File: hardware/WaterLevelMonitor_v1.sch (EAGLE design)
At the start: 38 parts, among them J1 D24V5F5, J2 AVR_SPI_PRG_6PTH, J5 D24V5F5, J6 D24V5F5, J7 RJ45, Q1 NDP6020P, Q4 2N3904, U1 ATMEGA328P_PDIP

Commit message: Add files via upload
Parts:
- added D2: (no value), adafruit:DIODEDO-1N4148
- added J8: (no value), SparkFun-Connectors:M04PTH
- added J9: (no value), SparkFun-Connectors:M03PTH
- D1: value (none) -> 1N5819-B; device adafruit:DIODEDO-1N4148 -> diode:1N5819-B
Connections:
- removed net BATSW: R3.2
- new net N$12: J3.7, U1.PD4(XCK/T0)
- new net N$13: D2.C, J8.2
- new net N$15: D2.A, U1.PD0(RXD)
- new net N$16: J3.9, U1.PD3(INT1)
- new net N$17: J3.10, U1.PD2(INT0)
- new net N$18: J8.1, J9.2
- new net N$19: R3.2, U1.PC5(ADC5/SCL)
- new net N$7: J8.3, U1.PD1(TXD)
- net GND: now also J3.2, J8.4
- net N$4: now also J3.12
- net N$6: now also U1.PC0(ADC0)
- net VCC: now also J9.1
- net VCEL: now also J3.1
- net VSEN: now also J9.3
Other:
- note added: "Bat GND SPKR+ SPKR- Rst PS Key RI TX RX NS Vio"
- note added: "Hardware UART"
- note added: "V+ RXD TXD GND"
- moved on the sheet: C2, C3, C4, J3, R6

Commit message: Add files via upload
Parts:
- removed C3: 10uF, SparkFun-Capacitors:CAP_POLPTH1
- removed C5: 470uF, SparkFun-Capacitors:CAP_POLPTH4
- removed D11, D7, D8, D9: 6V Zener, SparkFun-DiscreteSemi:DIODE-ZENERPTH
- removed J11: (no value), SparkFun-Connectors:M02PTH
- removed LED1: (no value), adafruit:LED5MM
- removed R10: 330, resistor:R-US_0204/5
- removed R12: 46K, resistor:R-US_0204/5
- added C11, C12, C13: 330uF, SparkFun-Capacitors:CAP_POLPTH1
- added J16: (no value), SparkFun-Connectors:M08SILK_FEMALE_PTH
- added JP1: JUMPER-PAD-2-NOYES_SILK, SparkFun-Passives:JUMPER-PAD-2-NOYES_SILK
- C4: value 100uF -> 330uF
- D3: value 1N4001 -> (none); device SparkFun-DiscreteSemi:DIODEPTH -> adafruit:DIODEDO-1N4148
- J4: device SparkFun-Connectors:M01PTH -> SparkFun-Connectors:M05PTH
- J8: device SparkFun-Connectors:M04PTH -> SparkFun-Connectors:M05PTH
- J9: device SparkFun-Connectors:M03PTH -> SparkFun-Connectors:M05PTH
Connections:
- removed net N$12: J3.7, U1.PD4(XCK/T0)
- removed net N$13: D2.C, J8.2
- removed net N$17: J3.10, U1.PD2(INT0)
- removed net N$18: J8.1, J9.2
- removed net N$4 (its old number): C10.+, C6.2, C9.+, D1.C, J3.12, U1.AVCC, U1.VCC
- removed net N$7: J8.3, U1.PD1(TXD)
- removed net N$8: C5.+
- new net HWRXD: D2.C, J4.3
- new net HWTXD: J4.4, U1.PD1(TXD)
- new net MISO: J2.1, U1.PB4(MISO)
- new net MOSI: J2.4, U1.PB3(MOSI/OC2)
- new net N$20: D3.A, U1.PC2(ADC2)
- new net N$21: D3.C, J9.3
- new net N$22: J9.4, U1.PC3(ADC3)
- new net N$25: J8.3, U1.PC4(ADC4/SDA)
- new net N$26: J8.4, U1.PC5(ADC5/SCL)
- new net N$27: J16.1, J7.1
- new net N$28: J16.2, J7.2
- new net N$29: J16.3, J7.3
- new net N$30: J16.4, J7.4
- new net N$31: J16.5, J7.5
- new net N$32: J2.5, U1.PC6(/RESET)
- new net N$33: J16.6, J7.6
- new net N$34: J16.7, J7.7
- new net N$35: J16.8, J7.8
- new net SCK: J2.3, U1.PB5(SCK)
- new net SS: U1.PB2(SS/OC1B)
- new net VMCU: D1.A, J1.4
- net GND: now also C11.-, C12.-, C13.-, J2.6, J4.5, J8.5, J9.5; no longer C3.-, C5.-, D11.A, D7.A, D8.A, D9.A, J11.1, J8.4, LED1.C, R12.1
- net N$1: now also J3.7, U1.PD5(T1); no longer LED1.A, R10.2
- net N$19: now also U1.PC1(ADC1); no longer U1.PC5(ADC5/SCL)
- net N$5: now also J3.10, U1.PD4(XCK/T0); no longer R12.2
- net VBAT: now also JP1.1
- net VBATSW: now also C13.+, C4.+
- net VCC: now also C10.+, C6.2, C9.+, D1.C, J2.2, J3.12, J4.2, J8.2, J9.2, U1.AVCC, U1.VCC; no longer D1.A, J1.4, J9.1
- net VCEL: now also C11.+, C12.+, JP1.2
- net VSEN: now also J4.1, J8.1, J9.1; no longer J9.3
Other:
- note added: "Debug Console"
- note added: "HW UART"
- note added: "I2C"
- note added: "VSEN VCC RXD TXD GND"
- note added: "VSEN VCC SDA SCL GND"
- note removed: "1 GND 2 RESET 3 VCC (5V) 4 motion detector 5 photocell 6 on/off button 7 UART Rx 8 UART Tx"
- note removed: "Hardware UART"
- note removed: "LED Indicators"
- note removed: "V+ RXD TXD GND"
- moved on the sheet: C2, C4, D2, D6, J1, J2, J3, J5, J6, J7, Q1, Q4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

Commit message: Add files via upload
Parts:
- added J10, J11: (no value), SparkFun-Connectors:M01PTH_NO_SILK_YES_STOP
- added J12: (no value), SparkFun-Connectors:M031X03_NO_SILK
- added J13, J14, J15: (no value), SparkFun-Connectors:M02PTH
- added J17: (no value), SparkFun-Connectors:M04X2
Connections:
- removed net SS: U1.PB2(SS/OC1B)
- new net N$13: J10.1, J3.6
- new net N$37: J12.2, U1.PD7(AIN1)
- new net N$38: J12.3, U1.PB0(ICP)
- new net N$5: J11.1, U1.PD2(INT0)
- new net N$8: J12.1, U1.PD6(AIN0)
- new net SS1: J17.5, U1.PB2(SS/OC1B)
- new net SS2: J17.7, U1.PB1(OC1A)
- net GND: now also J13.2, J14.2, J15.2, J17.6
- net MISO: now also J17.1
- net MOSI: now also J17.4
- net SCK: now also J17.3
- net VCC: now also J14.1, J17.2
- net VMCU: now also J15.1
- net VSEN: now also J13.1, J17.8
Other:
- note added: "SPI"
- moved on the sheet: J3, J4, J8, J9

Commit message: Add files via upload
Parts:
- removed C12, C13: 330uF, SparkFun-Capacitors:CAP_POLPTH1
- removed Q4: 2N3904, SparkFun-DiscreteSemi:TRANSISTOR_NPNTO-92-AMMO
- removed R7: 10K, resistor:R-US_0204/5
- added C3: 0.1uF, SparkFun-Capacitors:CAPPTH
- added C5: 20pF, SparkFun-Capacitors:CAPPTH
- added J18: (no value), SparkFun-Connectors:M02PTH
- added J19: (no value), SparkFun-Connectors:M01PTH_NO_SILK_YES_STOP
- added J20, J22: (no value), SparkFun-Connectors:M021X02_NO_SILK
- added LED1: (no value), led:LED5MM
- added Q3: NDP6020P, transistor-power:PMOSFET_PTO220BV
- added R2: 10K, resistor:R-US_0204/5
- added R4: 22K, resistor:R-US_0204/5
- C1: value 20pF -> 100uF; device SparkFun-Capacitors:CAPPTH -> SparkFun-Capacitors:CAP_POLPTH1
- C10: value 100uF -> 330uF
- C2: value 0.01uF -> 100uF; device SparkFun-Passives:CAPPTH1 -> SparkFun-Capacitors:CAP_POLPTH1
- C4: value 330uF -> 20pF; device SparkFun-Capacitors:CAP_POLPTH1 -> SparkFun-Capacitors:CAPPTH
- C6: value 0.1uF -> 0.01uF; device SparkFun-Capacitors:CAPPTH -> SparkFun-Passives:CAPPTH1
- C7: value 20pF -> 330uF; device SparkFun-Capacitors:CAPPTH -> SparkFun-Capacitors:CAP_POLPTH1
- C8: value 0.01uF -> 330uF; device SparkFun-Passives:CAPPTH1 -> SparkFun-Capacitors:CAP_POLPTH1
- C9: value 100uF -> 0.01uF; device SparkFun-Capacitors:CAP_POLPTH1 -> SparkFun-Passives:CAPPTH1
- J1: value D24V5F5 -> AVR_SPI_PRG_6PTH; device SparkFun-Connectors:M04PTH -> SparkFun-Connectors:AVR_SPI_PRG_6PTH
- J10: device SparkFun-Connectors:M01PTH_NO_SILK_YES_STOP -> SparkFun-Connectors:M12PTH
- J11: device SparkFun-Connectors:M01PTH_NO_SILK_YES_STOP -> SparkFun-Connectors:M02PTH
- J12: value (none) -> D24V5F5; device SparkFun-Connectors:M031X03_NO_SILK -> SparkFun-Connectors:M04PTH
- J13: device SparkFun-Connectors:M02PTH -> SparkFun-Connectors:M03PTH
- J14: device SparkFun-Connectors:M02PTH -> SparkFun-Connectors:M08SILK_FEMALE_PTH
- J15: device SparkFun-Connectors:M02PTH -> SparkFun-Connectors:M04X2
- J16: value (none) -> D24V5F5; device SparkFun-Connectors:M08SILK_FEMALE_PTH -> SparkFun-Connectors:M04PTH
- J17: value (none) -> RJ45; device SparkFun-Connectors:M04X2 -> SparkFun-Connectors:RJ45-8PTH
- J2: value AVR_SPI_PRG_6PTH -> (none); device SparkFun-Connectors:AVR_SPI_PRG_6PTH -> SparkFun-Connectors:M02PTH
- J3: device SparkFun-Connectors:M12PTH -> SparkFun-Connectors:M01PTH_NO_SILK_YES_STOP
- J4: device SparkFun-Connectors:M05PTH -> SparkFun-Connectors:M021X02_NO_SILK
- J5: value D24V5F5 -> (none); device SparkFun-Connectors:M04PTH -> SparkFun-Connectors:M01PTH_NO_SILK_YES_STOP
- J7: value RJ45 -> (none); device SparkFun-Connectors:RJ45-8PTH -> SparkFun-Connectors:M04PTH
- Q1: value NDP6020P -> (none); device transistor-power:PMOSFET_PTO220BV -> crystal:CRYSTALHC49U-V
- Q2: value (none) -> 2N3904; device crystal:CRYSTALHC49U-V -> SparkFun-DiscreteSemi:TRANSISTOR_NPNTO-92-AMMO
- R5: value 22K -> 10K
- R6: value 10K -> 330
- renumbered D6 to D4, X2 to X1
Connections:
- removed net N$37: J12.2, U1.PD7(AIN1)
- removed net N$38: J12.3, U1.PB0(ICP)
- new net N$12: LED1.A, R6.1
- new net PB0: J4.1, U1.PB0(ICP)
- new net PD6: J20.1, U1.PD6(AIN0)
- new net PD7: J22.1, U1.PD7(AIN1)
- net GND: now also C1.-, C2.-, C3.1, C4.1, C5.1, C7.-, C8.-, C9.2, J1.6, J10.2, J11.2, J12.3, J15.6, J16.3, J18.2, J2.1, J20.2, J22.2, J4.2, J7.4, LED1.C, Q2.E, R5.1; no longer C1.1, C12.-, C13.-, C2.2, C4.-, C7.1, C8.1, C9.-, J1.3, J14.2, J15.2, J17.6, J2.6, J3.2, J4.5, J5.3, Q4.E, R6.1
- net HWRXD: now also D3.C, J9.3; no longer D2.C, J4.3
- net HWTXD: now also J9.4; no longer J4.4
- net MISO: now also J1.1, J15.1; no longer J17.1, J2.1
- net MOSI: now also J1.4, J15.4; no longer J17.4, J2.4
- net N$1: now also J10.7; no longer J3.7
- net N$10: now also C5.2, Q1.1; no longer C7.2, Q2.1
- net N$11: now also C6.2; no longer C8.2
- net N$13: now also J10.6, J5.1; no longer J10.1, J3.6
- net N$14: now also Q2.C, R3.1; no longer Q4.C, R7.1
- net N$15: now also D3.A; no longer D2.A
- net N$19: now also R1.2; no longer R3.2
- net N$2: now also Q3.G, R2.1, R3.2; no longer Q1.G, R1.1, R7.2
- net N$20: now also D2.A; no longer D3.A
- net N$21: now also D2.C, J7.2; no longer D3.C, J9.3
- net N$22: now also J7.3; no longer J9.4
- net N$27: now also J14.1, J17.1; no longer J16.1, J7.1
- net N$28: now also J14.2, J17.2; no longer J16.2, J7.2
- net N$29: now also J14.3, J17.3; no longer J16.3, J7.3
- net N$3: now also Q2.B, R1.1; no longer Q4.B, R3.1
- net N$30: now also J14.4, J17.4; no longer J16.4, J7.4
- net N$31: now also J14.5, J17.5; no longer J16.5, J7.5
- net N$32: now also J1.5; no longer J2.5
- net N$33: now also J14.6, J17.6; no longer J16.6, J7.6
- net N$34: now also J14.7, J17.7; no longer J16.7, J7.7
- net N$35: now also J14.8, J17.8; no longer J16.8, J7.8
- net N$4: now also J10.9; no longer J3.9
- net N$5: now also J3.1; no longer J11.1
- net N$6: now also C9.1, R4.1, R5.2; no longer C2.1, R5.1, R6.2
- net N$7: now also J10.10; no longer J3.10
- net N$8: now also J19.1, R6.2; no longer J12.1, U1.PD6(AIN0)
- net N$9: now also C4.2, Q1.2; no longer C1.2, Q2.2
- net SCK: now also J1.3, J15.3; no longer J17.3, J2.3
- net SS1: now also J15.5; no longer J17.5
- net SS2: now also J15.7; no longer J17.7
- net VBAT: now also J2.2, J6.2, Q3.S, R2.2; no longer J1.2, Q1.S, R1.2
- net VBATSW: now also C10.+, C11.+, J12.2, J16.2, Q3.D, R4.2; no longer C13.+, C4.+, J5.2, J6.2, Q1.D, R5.2
- net VCC: now also D1.A, J1.2, J10.12, J11.1, J13.1, J15.2, J6.4, J7.1; no longer C10.+, C6.2, C9.+, D1.C, J14.1, J17.2, J2.2, J3.12, J4.2, U1.AVCC, U1.VCC
- net VCEL: now also C7.+, C8.+, J10.1, J12.4; no longer C11.+, C12.+, J3.1, J5.4
- net VMCU: now also C1.+, C2.+, C3.2, D1.C, U1.AVCC, U1.VCC; no longer D1.A, J1.4, J15.1
- net VSEN: now also J13.3, J15.8, J16.4, J18.1; no longer J13.1, J17.8, J4.1, J6.4
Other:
- note added: "VCC RXD TXD GND"
- moved on the sheet: C10, C11, C6, D2, D3, J6, J9, R1, R3, R5, R6

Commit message: Add files via upload
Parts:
- removed X1: (no value), con-wago-500:W237-102
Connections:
- net GND: no longer X1-2.KL
- net VBAT: no longer X1-1.KL
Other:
- note added: "Battery In (5-9VDC)"
- note removed: "Battery 12V"
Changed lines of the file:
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@@
 <part name="Q2" library="SparkFun-DiscreteSemi" deviceset="TRANSISTOR_NPN" device="TO-92-AMMO" value="2N3904"/>
 <part name="R2" library="resistor" deviceset="R-US_" device="0204/5" value="10K"/>
-<part name="X1" library="con-wago-500" deviceset="W237-102" device=""/>
 <part name="R1" library="resistor" deviceset="R-US_" device="0204/5" value="10K"/>
 <part name="GND9" library="SparkFun-Aesthetics" deviceset="GND" device=""/>
-<part name="GND11" library="SparkFun-Aesthetics" deviceset="GND" device=""/>
 <part name="C9" library="SparkFun-Passives" deviceset="CAP" device="PTH1" value="0.01uF"/>
 <part name="R4" library="resistor" deviceset="R-US_" device="0204/5" value="22K"/>
@@
 <sheet>
 <plain>
-<text x="0" y="241.3" size="1.778" layer="91">Battery
-12V</text>
+<text x="-60.96" y="228.6" size="1.778" layer="91">Battery
+In (5-9VDC)</text>
 <wire x1="-137.16" y1="144.78" x2="-96.52" y2="144.78" width="0.1524" layer="97" style="longdash"/>
 <wire x1="-96.52" y1="144.78" x2="-96.52" y2="114.3" width="0.1524" layer="97" style="longdash"/>
@@
 <instance part="Q2" gate="G$1" x="-12.7" y="185.42"/>
 <instance part="R2" gate="G$1" x="-10.16" y="210.82" rot="R90"/>
-<instance part="X1" gate="-1" x="7.62" y="233.68" rot="R270"/>
-<instance part="X1" gate="-2" x="2.54" y="233.68" rot="R270"/>
 <instance part="R1" gate="G$1" x="-22.86" y="185.42" rot="R180"/>
 <instance part="GND9" gate="1" x="-10.16" y="175.26"/>
-<instance part="GND11" gate="1" x="2.54" y="223.52"/>
 <instance part="C9" gate="G$1" x="15.24" y="160.02"/>
 <instance part="R4" gate="G$1" x="7.62" y="182.88" rot="R90"/>
@@
 <net name="GND" class="0">
 <segment>
-<pinref part="GND11" gate="1" pin="GND"/>
-<pinref part="X1" gate="-2" pin="KL"/>
-<wire x1="2.54" y1="226.06" x2="2.54" y2="228.6" width="0.1524" layer="91"/>
-</segment>
-<segment>
 <pinref part="Q2" gate="G$1" pin="E"/>
 <pinref part="GND9" gate="1" pin="GND"/>
@@
 <net name="VBAT" class="0">
 <segment>
-<pinref part="X1" gate="-1" pin="KL"/>
 <pinref part="Q3" gate="G$1" pin="S"/>
-<wire x1="7.62" y1="228.6" x2="7.62" y2="218.44" width="0.1524" layer="91"/>
 <pinref part="R2" gate="G$1" pin="2"/>
 <wire x1="7.62" y1="218.44" x2="7.62" y2="205.74" width="0.1524" layer="91"/>

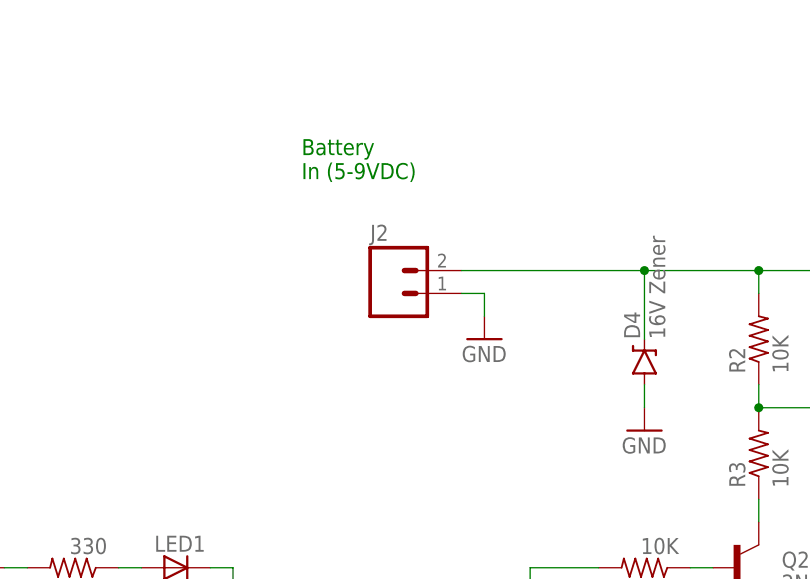
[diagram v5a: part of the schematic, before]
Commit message: added DC power jack
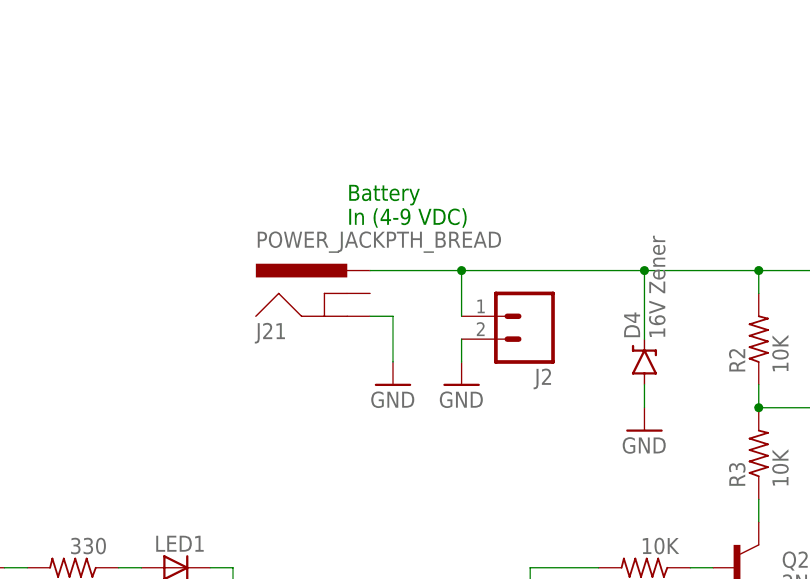
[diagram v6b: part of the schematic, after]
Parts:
- added J21: POWER_JACKPTH_BREAD, SparkFun-Connectors:POWER_JACKPTH_BREAD
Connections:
- net GND: now also J2.2, J21.GND; no longer J2.1
- net VBAT: now also J2.1, J21.PWR; no longer J2.2
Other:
- note added: "Battery In (4-9 VDC)"
- note removed: "Battery In (5-9VDC)"
- moved on the sheet: J2
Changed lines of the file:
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@@
 <part name="J13" library="SparkFun-Connectors" deviceset="M03" device="PTH"/>
 <part name="GND21" library="SparkFun-Aesthetics" deviceset="GND" device=""/>
-<part name="J2" library="SparkFun-Connectors" deviceset="M02" device="PTH"/>
 <part name="GND7" library="SparkFun-Aesthetics" deviceset="GND" device=""/>
 <part name="GND28" library="SparkFun-Aesthetics" deviceset="GND" device=""/>
@@
 <part name="LED1" library="led" deviceset="LED" device="5MM"/>
 <part name="J19" library="SparkFun-Connectors" deviceset="M01" device="PTH_NO_SILK_YES_STOP"/>
+<part name="J2" library="SparkFun-Connectors" deviceset="M02" device="PTH"/>
+<part name="GND11" library="SparkFun-Aesthetics" deviceset="GND" device=""/>
+<part name="J21" library="SparkFun-Connectors" deviceset="POWER_JACK" device="PTH_BREAD"/>
 </parts>
 <sheets>
 <sheet>
 <plain>
-<text x="-60.96" y="228.6" size="1.778" layer="91">Battery
-In (5-9VDC)</text>
+<text x="-55.88" y="223.52" size="1.778" layer="91">Battery
+In (4-9 VDC)</text>
 <wire x1="-137.16" y1="144.78" x2="-96.52" y2="144.78" width="0.1524" layer="97" style="longdash"/>
 <wire x1="-96.52" y1="144.78" x2="-96.52" y2="114.3" width="0.1524" layer="97" style="longdash"/>
@@
 <instance part="J13" gate="J$1" x="66.04" y="154.94" rot="R180"/>
 <instance part="GND21" gate="1" x="40.64" y="149.86"/>
-<instance part="J2" gate="G$1" x="-50.8" y="215.9"/>
-<instance part="GND7" gate="1" x="-40.64" y="210.82"/>
+<instance part="GND7" gate="1" x="-50.8" y="205.74"/>
 <instance part="GND28" gate="1" x="71.12" y="104.14"/>
 <instance part="GND29" gate="1" x="71.12" y="91.44"/>
@@
 <instance part="LED1" gate="G$1" x="-76.2" y="185.42" rot="R90"/>
 <instance part="J19" gate="G$1" x="-101.6" y="185.42"/>
+<instance part="J2" gate="G$1" x="-35.56" y="213.36" rot="R180"/>
+<instance part="GND11" gate="1" x="-43.18" y="205.74"/>
+<instance part="J21" gate="G$1" x="-55.88" y="210.82"/>
 </instances>
 <busses>
@@
 </segment>
 <segment>
-<pinref part="J2" gate="G$1" pin="1"/>
 <pinref part="GND7" gate="1" pin="GND"/>
-<wire x1="-43.18" y1="215.9" x2="-40.64" y2="215.9" width="0.1524" layer="91"/>
-<wire x1="-40.64" y1="215.9" x2="-40.64" y2="213.36" width="0.1524" layer="91"/>
+<wire x1="-53.34" y1="213.36" x2="-50.8" y2="213.36" width="0.1524" layer="91"/>
+<wire x1="-50.8" y1="213.36" x2="-50.8" y2="208.28" width="0.1524" layer="91"/>
+<pinref part="J21" gate="G$1" pin="GND"/>
 </segment>
 <segment>
@@
 <wire x1="-71.12" y1="185.42" x2="-68.58" y2="185.42" width="0.1524" layer="91"/>
 <wire x1="-68.58" y1="185.42" x2="-68.58" y2="182.88" width="0.1524" layer="91"/>
+</segment>
+<segment>
+<pinref part="J2" gate="G$1" pin="2"/>
+<pinref part="GND11" gate="1" pin="GND"/>
+<wire x1="-43.18" y1="210.82" x2="-43.18" y2="208.28" width="0.1524" layer="91"/>
 </segment>
 </net>
@@
 <wire x1="20.32" y1="241.3" x2="25.4" y2="241.3" width="0.1524" layer="91"/>
 <junction x="20.32" y="218.44"/>
-<pinref part="J2" gate="G$1" pin="2"/>
+<wire x1="-53.34" y1="218.44" x2="-43.18" y2="218.44" width="0.1524" layer="91"/>
+<junction x="-22.86" y="218.44"/>
+<pinref part="J2" gate="G$1" pin="1"/>
 <wire x1="-43.18" y1="218.44" x2="-22.86" y2="218.44" width="0.1524" layer="91"/>
-<junction x="-22.86" y="218.44"/>
+<wire x1="-43.18" y1="213.36" x2="-43.18" y2="218.44" width="0.1524" layer="91"/>
+<junction x="-43.18" y="218.44"/>
+<pinref part="J21" gate="G$1" pin="PWR"/>
 </segment>
 </net>

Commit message: Add files via upload
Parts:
- added J23: (no value), SparkFun-Connectors:M01PTH_NO_SILK_YES_STOP
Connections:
- new net N$16: J21.GNDBREAK, J23.1
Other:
- moved on the sheet: J21
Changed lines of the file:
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@@
 <part name="GND11" library="SparkFun-Aesthetics" deviceset="GND" device=""/>
 <part name="J21" library="SparkFun-Connectors" deviceset="POWER_JACK" device="PTH_BREAD"/>
+<part name="J23" library="SparkFun-Connectors" deviceset="M01" device="PTH_NO_SILK_YES_STOP"/>
 </parts>
 <sheets>
 <sheet>
 <plain>
-<text x="-55.88" y="223.52" size="1.778" layer="91">Battery
-In (4-9 VDC)</text>
+<text x="-101.6" y="215.9" size="1.778" layer="91">Battery In
+(4-9 VDC)</text>
 <wire x1="-137.16" y1="144.78" x2="-96.52" y2="144.78" width="0.1524" layer="97" style="longdash"/>
 <wire x1="-96.52" y1="144.78" x2="-96.52" y2="114.3" width="0.1524" layer="97" style="longdash"/>
@@
 <instance part="J13" gate="J$1" x="66.04" y="154.94" rot="R180"/>
 <instance part="GND21" gate="1" x="40.64" y="149.86"/>
-<instance part="GND7" gate="1" x="-50.8" y="205.74"/>
+<instance part="GND7" gate="1" x="-66.04" y="205.74"/>
 <instance part="GND28" gate="1" x="71.12" y="104.14"/>
 <instance part="GND29" gate="1" x="71.12" y="91.44"/>
@@
 <instance part="J2" gate="G$1" x="-35.56" y="213.36" rot="R180"/>
 <instance part="GND11" gate="1" x="-43.18" y="205.74"/>
-<instance part="J21" gate="G$1" x="-55.88" y="210.82"/>
+<instance part="J21" gate="G$1" x="-73.66" y="210.82"/>
+<instance part="J23" gate="G$1" x="-53.34" y="213.36" rot="R180"/>
 </instances>
 <busses>
@@
 <segment>
 <pinref part="GND7" gate="1" pin="GND"/>
-<wire x1="-53.34" y1="213.36" x2="-50.8" y2="213.36" width="0.1524" layer="91"/>
-<wire x1="-50.8" y1="213.36" x2="-50.8" y2="208.28" width="0.1524" layer="91"/>
+<wire x1="-71.12" y1="213.36" x2="-66.04" y2="213.36" width="0.1524" layer="91"/>
+<wire x1="-66.04" y1="213.36" x2="-66.04" y2="208.28" width="0.1524" layer="91"/>
 <pinref part="J21" gate="G$1" pin="GND"/>
 </segment>
@@
 <wire x1="20.32" y1="241.3" x2="25.4" y2="241.3" width="0.1524" layer="91"/>
 <junction x="20.32" y="218.44"/>
-<wire x1="-53.34" y1="218.44" x2="-43.18" y2="218.44" width="0.1524" layer="91"/>
+<wire x1="-71.12" y1="218.44" x2="-43.18" y2="218.44" width="0.1524" layer="91"/>
 <junction x="-22.86" y="218.44"/>
 <pinref part="J2" gate="G$1" pin="1"/>
@@
 </segment>
 </net>
+<net name="N$16" class="0">
+<segment>
+<pinref part="J21" gate="G$1" pin="GNDBREAK"/>
+<pinref part="J23" gate="G$1" pin="1"/>
+<wire x1="-71.12" y1="215.9" x2="-60.96" y2="215.9" width="0.1524" layer="91"/>
+<wire x1="-60.96" y1="215.9" x2="-60.96" y2="213.36" width="0.1524" layer="91"/>
+</segment>
+</net>
